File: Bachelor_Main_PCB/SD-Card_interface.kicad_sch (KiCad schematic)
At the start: 1 part, among them J16 F32Q-1A7H1-11022

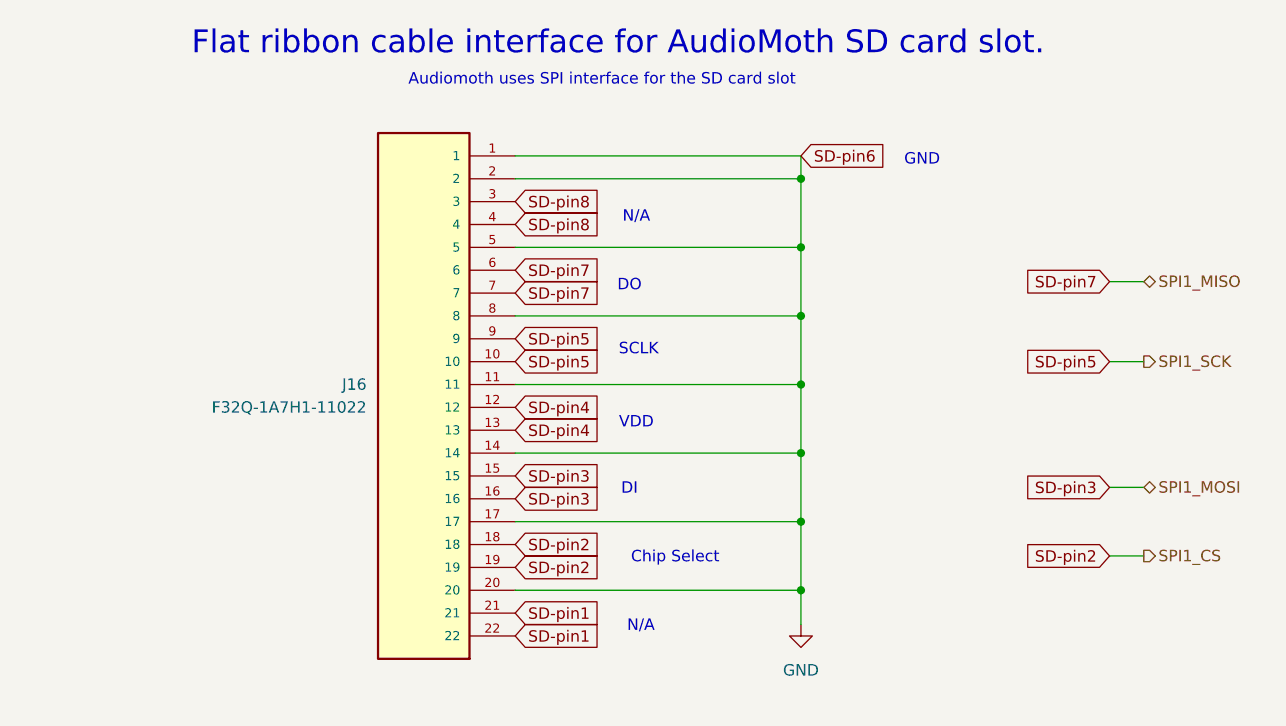
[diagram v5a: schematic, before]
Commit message: Achematic review changes. Smal ones. Replaced TX_ON LED
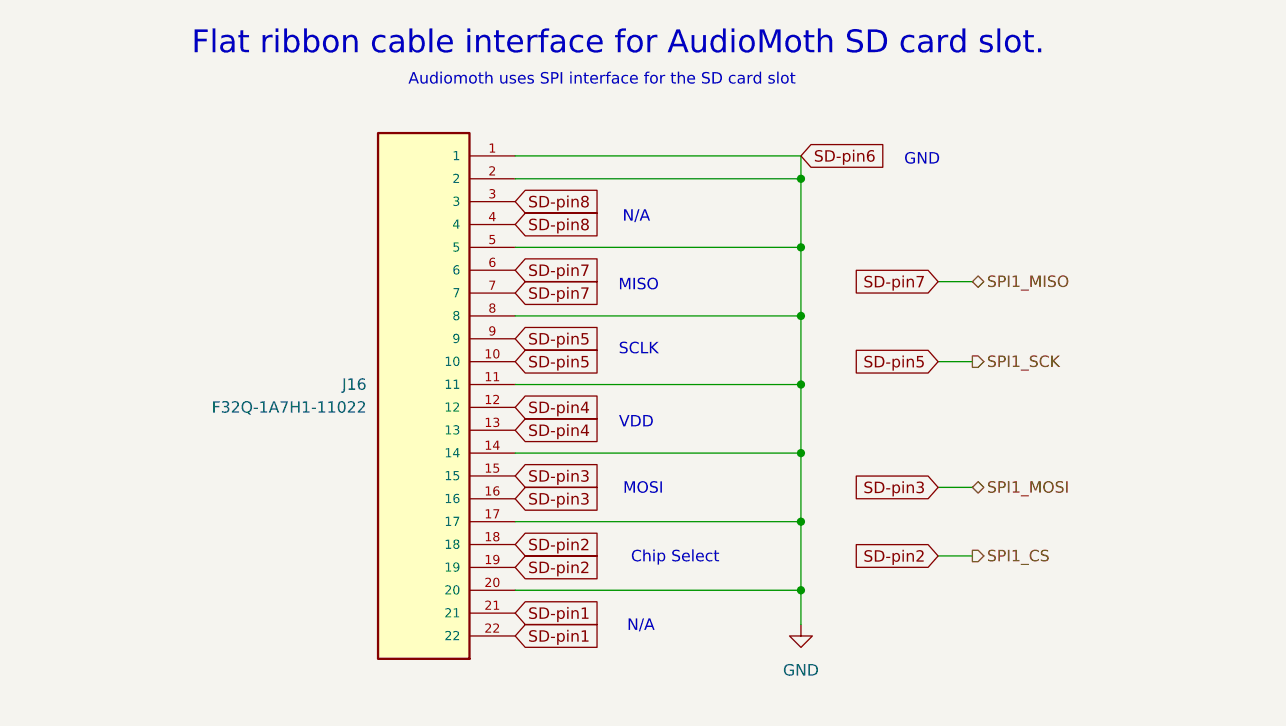
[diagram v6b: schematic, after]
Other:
- note added: "MISO"
- note added: "MOSI"
- note removed: "DI"
- note removed: "DO"
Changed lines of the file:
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@@
 		)
 	)
-	(text "DO"
+	(text "MISO"
 		(exclude_from_sim no)
-		(at 127 71.628 0)
+		(at 128.016 71.628 0)
 		(effects
 			(font
@@
 		)
 	)
-	(text "DI"
+	(text "MOSI"
 		(exclude_from_sim no)
-		(at 127 94.234 0)
+		(at 128.524 94.234 0)
 		(effects
 			(font
@@
 	(wire
 		(pts
-			(xy 180.34 80.01) (xy 184.15 80.01)
+			(xy 161.29 80.01) (xy 165.1 80.01)
 		)
 		(stroke
@@
 	(wire
 		(pts
-			(xy 184.15 101.6) (xy 180.34 101.6)
+			(xy 165.1 101.6) (xy 161.29 101.6)
 		)
 		(stroke
@@
 	(wire
 		(pts
-			(xy 180.34 71.12) (xy 184.15 71.12)
+			(xy 161.29 71.12) (xy 165.1 71.12)
 		)
 		(stroke
@@
 	(wire
 		(pts
-			(xy 180.34 93.98) (xy 184.15 93.98)
+			(xy 161.29 93.98) (xy 165.1 93.98)
 		)
 		(stroke
@@
 	(global_label "SD-pin7"
 		(shape input)
-		(at 180.34 71.12 180)
+		(at 161.29 71.12 180)
 		(fields_autoplaced yes)
 		(effects
@@
 		)
 		(property "Intersheetrefs" "${INTERSHEET_REFS}"
-			(at 169.1906 71.12 0)
+			(at 150.1406 71.12 0)
 			(effects
 				(font
@@
 	(global_label "SD-pin2"
 		(shape input)
-		(at 180.34 101.6 180)
+		(at 161.29 101.6 180)
 		(fields_autoplaced yes)
 		(effects
@@
 		)
 		(property "Intersheetrefs" "${INTERSHEET_REFS}"
-			(at 169.1906 101.6 0)
+			(at 150.1406 101.6 0)
 			(effects
 				(font
@@
 	(global_label "SD-pin3"
 		(shape input)
-		(at 180.34 93.98 180)
+		(at 161.29 93.98 180)
 		(fields_autoplaced yes)
 		(effects
@@
 		)
 		(property "Intersheetrefs" "${INTERSHEET_REFS}"
-			(at 169.1906 93.98 0)
+			(at 150.1406 93.98 0)
 			(effects
 				(font
@@
 	(global_label "SD-pin5"
 		(shape input)
-		(at 180.34 80.01 180)
+		(at 161.29 80.01 180)
 		(fields_autoplaced yes)
 		(effects
@@
 		)
 		(property "Intersheetrefs" "${INTERSHEET_REFS}"
-			(at 169.1906 80.01 0)
+			(at 150.1406 80.01 0)
 			(effects
 				(font
@@
 	(hierarchical_label "SPI1_MOSI"
 		(shape bidirectional)
-		(at 184.15 93.98 0)
+		(at 165.1 93.98 0)
 		(effects
 			(font
@@
 	(hierarchical_label "SPI1_SCK"
 		(shape output)
-		(at 184.15 80.01 0)
+		(at 165.1 80.01 0)
 		(effects
 			(font
@@
 	(hierarchical_label "SPI1_CS"
 		(shape output)
-		(at 184.15 101.6 0)
+		(at 165.1 101.6 0)
 		(effects
 			(font
@@
 	(hierarchical_label "SPI1_MISO"
 		(shape bidirectional)
-		(at 184.15 71.12 0)
-		(effects
-			(font
+		(at 165.1 71.12 0)
+		(effects
+			(font

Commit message: Updated the "Part-no" field in the symbol field table for all components
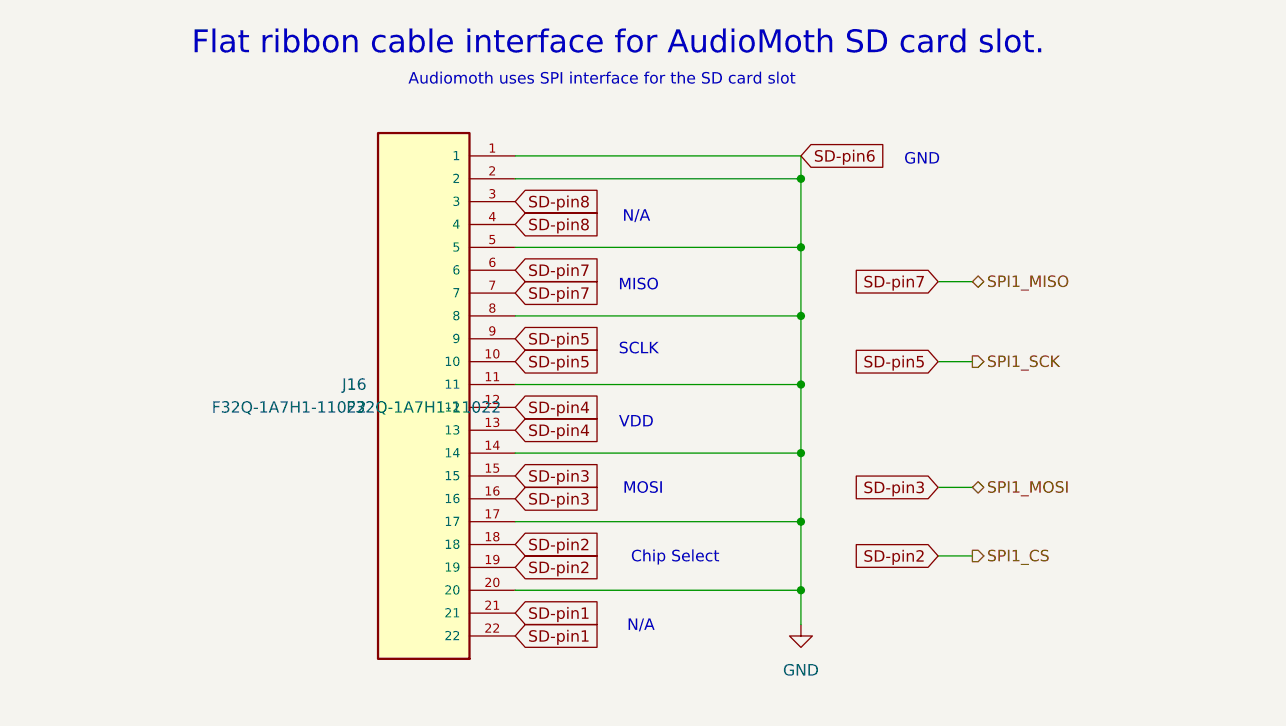
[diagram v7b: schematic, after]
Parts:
- J16: Part-no (none) -> F32Q-1A7H1-11022
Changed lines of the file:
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@@
+			)
+		)
+		(property "Part-no" "F32Q-1A7H1-11022"
+			(at 104.14 85.09 0)
+			(effects
+				(font
+					(size 1.27 1.27)
+				)
 			)
 		)

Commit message: Add 1% tolerance field to high tolerance resistors
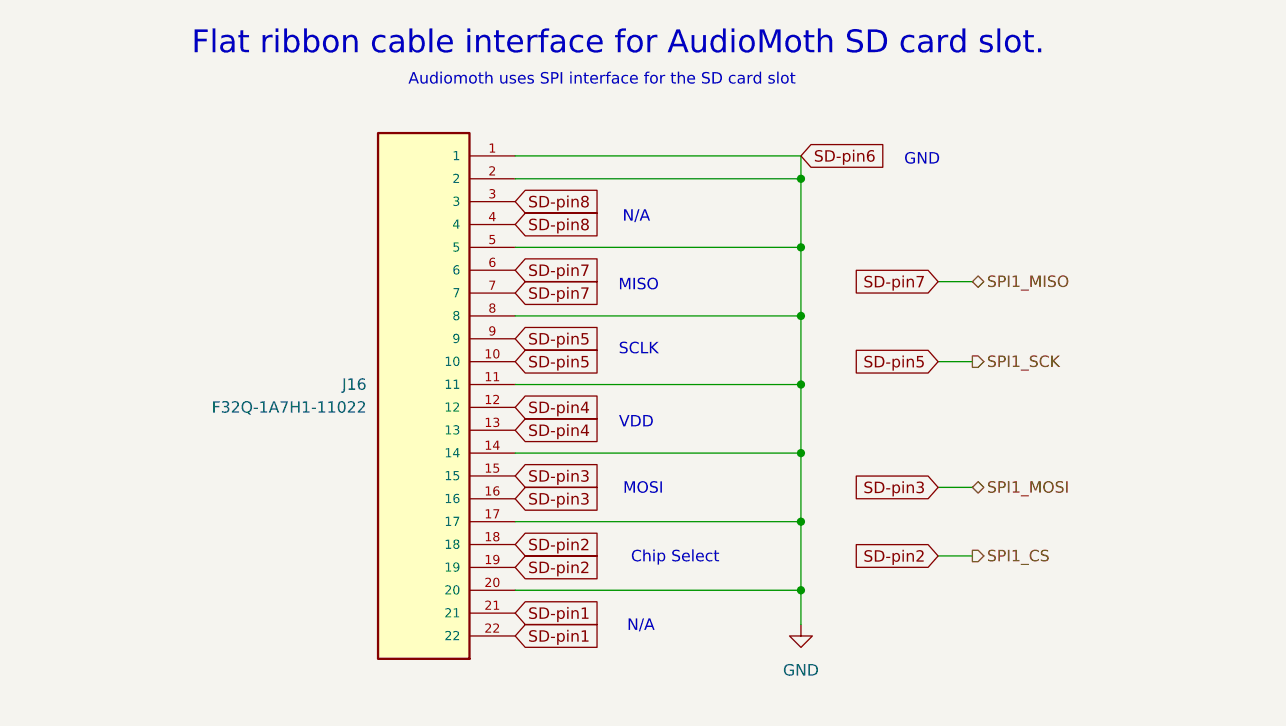
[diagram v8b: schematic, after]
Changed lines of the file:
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@@
 					(size 1.27 1.27)
 				)
+				(hide yes)
 			)
 		)
